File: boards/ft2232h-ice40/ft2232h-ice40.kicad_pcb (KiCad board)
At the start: 4 copper layers, 34 x 22.4 mm, 36 parts, among them J1 USB_B_Micro, J2 Conn_01x08, U1 AP7361C_SOT-89-5, U2 FT2232H, X1 ASEM1-12.000MHZ

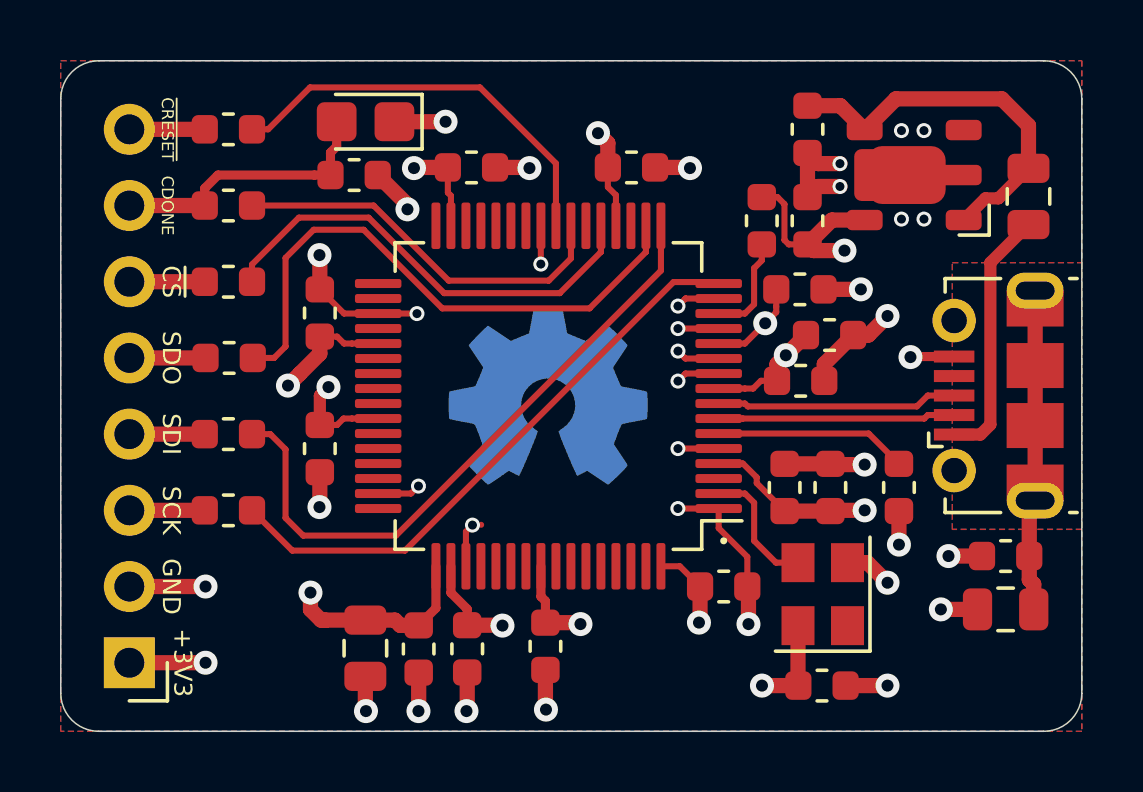
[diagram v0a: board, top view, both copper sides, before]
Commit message: Revert "Updated version info on backside of board."
This reverts commit 1f51933b87c9f3e20d21da3a8fb08a06faebd8ba.
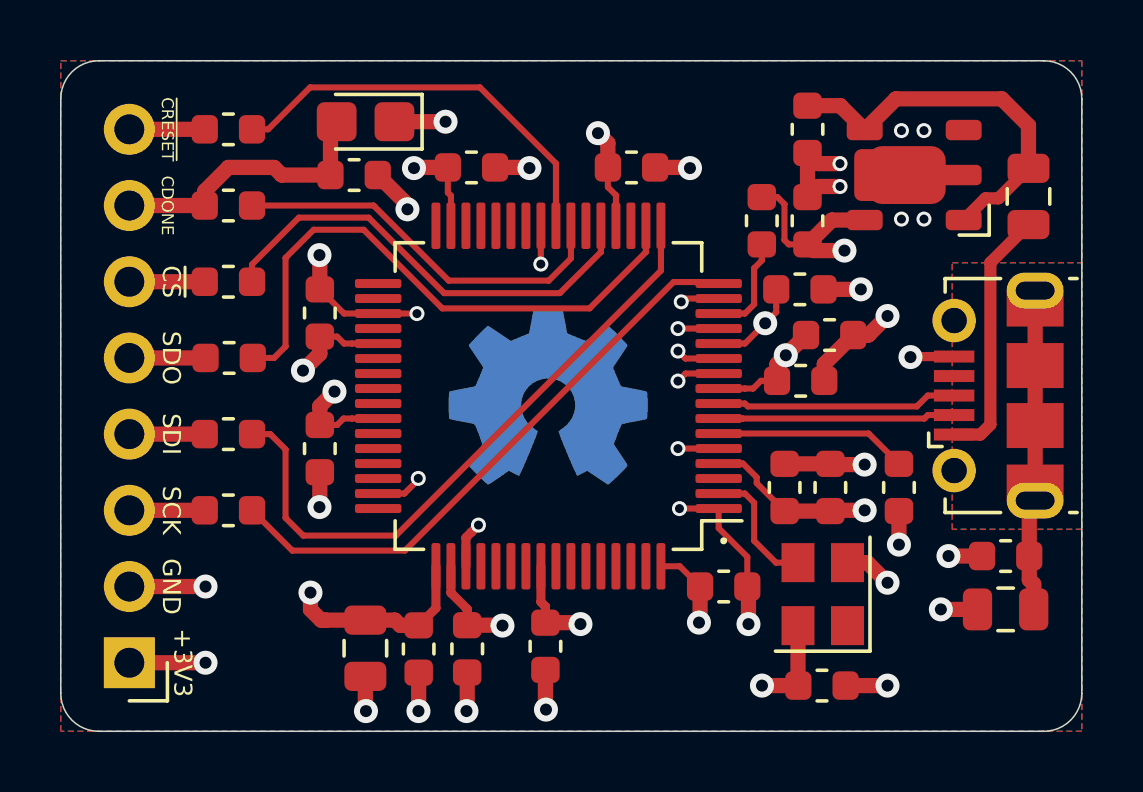
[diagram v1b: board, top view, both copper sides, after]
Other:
- board text removed: "ft2232h-ice40 2020-02 fourside.io"

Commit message: Updated version info on backside of board.
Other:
- board text added: "ft2232h-ice40 2020-02 fourside.io"
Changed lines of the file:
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@@
   (general
     (thickness 1.6)
-    (drawings 17)
+    (drawings 18)
     (tracks 305)
     (zones 0)
@@
   )
   (setup
-    (last_trace_width 0.3048)
+    (last_trace_width 0.1524)
     (user_trace_width 0.2032)
     (user_trace_width 0.3048)
@@
       (rotate (xyz 0 0 0))
     )
+  )
+  (gr_text "ft2232h-ice40\n2020-02\nfourside.io" (at 55.05 35.55) (layer B.Mask)
+    (effects (font (size 1 1) (thickness 0.15)) (justify right mirror))
   )
   (gr_arc (start 82.042 38.353999) (end 82.042 39.624) (angle -90) (layer Edge.Cuts) (width 0.05))
@@
   (segment (start 71.207 24.698) (end 71.157399 24.648399) (width 0.2032) (layer F.Cu) (net 15))
   (segment (start 71.157399 24.648399) (end 69.701601 24.648399) (width 0.2032) (layer F.Cu) (net 15))
-  (segment (start 76.2055 29.698) (end 71.207 29.698) (width 0.2032) (layer F.Cu) (net 55))
-  (segment (start 77.216 30.7085) (end 76.2055 29.698) (width 0.2032) (layer F.Cu) (net 55))
   (segment (start 69.282 23.648) (end 69.282 22.773) (width 0.2032) (layer F.Cu) (net 16))
   (segment (start 69.282 24.268) (end 69.282 23.648) (width 0.2032) (layer F.Cu) (net 16))
@@
   (segment (start 67.282 22.773) (end 67.282 23.648) (width 0.2032) (layer F.Cu) (net 18))
   (segment (start 57.213289 22.501211) (end 55.6515 24.063) (width 0.2032) (layer F.Cu) (net 18))
+  (segment (start 73.118 34.002) (end 73.851 34.002) (width 0.2032) (layer F.Cu) (net 52))
+  (segment (start 72.39 33.274) (end 73.118 34.002) (width 0.2032) (layer F.Cu) (net 52))
+  (segment (start 72.39 32.006) (end 72.39 33.274) (width 0.2032) (layer F.Cu) (net 52))
+  (segment (start 71.207 31.698) (end 72.082 31.698) (width 0.2032) (layer F.Cu) (net 52))
+  (segment (start 72.082 31.698) (end 72.39 32.006) (width 0.2032) (layer F.Cu) (net 52))
+  (segment (start 81.5595 33.782) (end 81.5595 34.5695) (width 0.508) (layer F.Cu) (net 54))
+  (segment (start 81.7095 34.7195) (end 81.7095 35.56) (width 0.508) (layer F.Cu) (net 54))
+  (segment (start 81.5595 34.5695) (end 81.7095 34.7195) (width 0.508) (layer F.Cu) (net 54))
+  (segment (start 81.5595 31.528) (end 81.7555 31.332) (width 0.508) (layer F.Cu) (net 54))
+  (segment (start 81.5595 33.782) (end 81.5595 31.528) (width 0.508) (layer F.Cu) (net 54))
+  (segment (start 81.7555 31.332) (end 81.7555 29.432) (width 0.508) (layer F.Cu) (net 54))
+  (segment (start 81.7555 29.432) (end 81.7555 27.432) (width 0.508) (layer F.Cu) (net 54))
+  (segment (start 81.7555 27.432) (end 81.7555 25.532) (width 0.508) (layer F.Cu) (net 54))
+  (segment (start 76.2055 29.698) (end 71.207 29.698) (width 0.2032) (layer F.Cu) (net 55))
+  (segment (start 77.216 30.7085) (end 76.2055 29.698) (width 0.2032) (layer F.Cu) (net 55))
+  (segment (start 72.644 23.931) (end 72.644 23.3935) (width 0.2032) (layer F.Cu) (net 56))
+  (segment (start 72.38739 24.18761) (end 72.644 23.931) (width 0.2032) (layer F.Cu) (net 56))
+  (segment (start 72.38739 25.39261) (end 72.38739 24.18761) (width 0.2032) (layer F.Cu) (net 56))
+  (segment (start 71.207 25.698) (end 72.082 25.698) (width 0.2032) (layer F.Cu) (net 56))
+  (segment (start 72.082 25.698) (end 72.38739 25.39261) (width 0.2032) (layer F.Cu) (net 56))
   (segment (start 66.282 22.773) (end 66.282 23.86237) (width 0.2032) (layer F.Cu) (net 57))
   (segment (start 59.70506 22.098) (end 55.6515 22.098) (width 0.2032) (layer F.Cu) (net 57))
@@
   (segment (start 65.782 22.773) (end 65.782 20.69363) (width 0.2032) (layer F.Cu) (net 58))
   (segment (start 65.782 20.69363) (end 63.24937 18.161) (width 0.2032) (layer F.Cu) (net 58))
-  (segment (start 73.118 34.002) (end 73.851 34.002) (width 0.2032) (layer F.Cu) (net 52))
-  (segment (start 72.39 33.274) (end 73.118 34.002) (width 0.2032) (layer F.Cu) (net 52))
-  (segment (start 72.39 32.006) (end 72.39 33.274) (width 0.2032) (layer F.Cu) (net 52))
-  (segment (start 71.207 31.698) (end 72.082 31.698) (width 0.2032) (layer F.Cu) (net 52))
-  (segment (start 72.082 31.698) (end 72.39 32.006) (width 0.2032) (layer F.Cu) (net 52))
-  (segment (start 72.644 23.931) (end 72.644 23.3935) (width 0.2032) (layer F.Cu) (net 56))
-  (segment (start 72.38739 24.18761) (end 72.644 23.931) (width 0.2032) (layer F.Cu) (net 56))
-  (segment (start 72.38739 25.39261) (end 72.38739 24.18761) (width 0.2032) (layer F.Cu) (net 56))
-  (segment (start 71.207 25.698) (end 72.082 25.698) (width 0.2032) (layer F.Cu) (net 56))
-  (segment (start 72.082 25.698) (end 72.38739 25.39261) (width 0.2032) (layer F.Cu) (net 56))
-  (segment (start 81.5595 33.782) (end 81.5595 34.5695) (width 0.508) (layer F.Cu) (net 54))
-  (segment (start 81.7095 34.7195) (end 81.7095 35.56) (width 0.508) (layer F.Cu) (net 54))
-  (segment (start 81.5595 34.5695) (end 81.7095 34.7195) (width 0.508) (layer F.Cu) (net 54))
-  (segment (start 81.5595 31.528) (end 81.7555 31.332) (width 0.508) (layer F.Cu) (net 54))
-  (segment (start 81.5595 33.782) (end 81.5595 31.528) (width 0.508) (layer F.Cu) (net 54))
-  (segment (start 81.7555 31.332) (end 81.7555 29.432) (width 0.508) (layer F.Cu) (net 54))
-  (segment (start 81.7555 29.432) (end 81.7555 27.432) (width 0.508) (layer F.Cu) (net 54))
-  (segment (start 81.7555 27.432) (end 81.7555 25.532) (width 0.508) (layer F.Cu) (net 54))
   (zone (net 4) (net_name +3V3) (layer In1.Cu) (hatch edge 0.508)
     (connect_pads (clearance 0.1524))
